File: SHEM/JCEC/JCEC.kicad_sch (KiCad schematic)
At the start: 0 parts

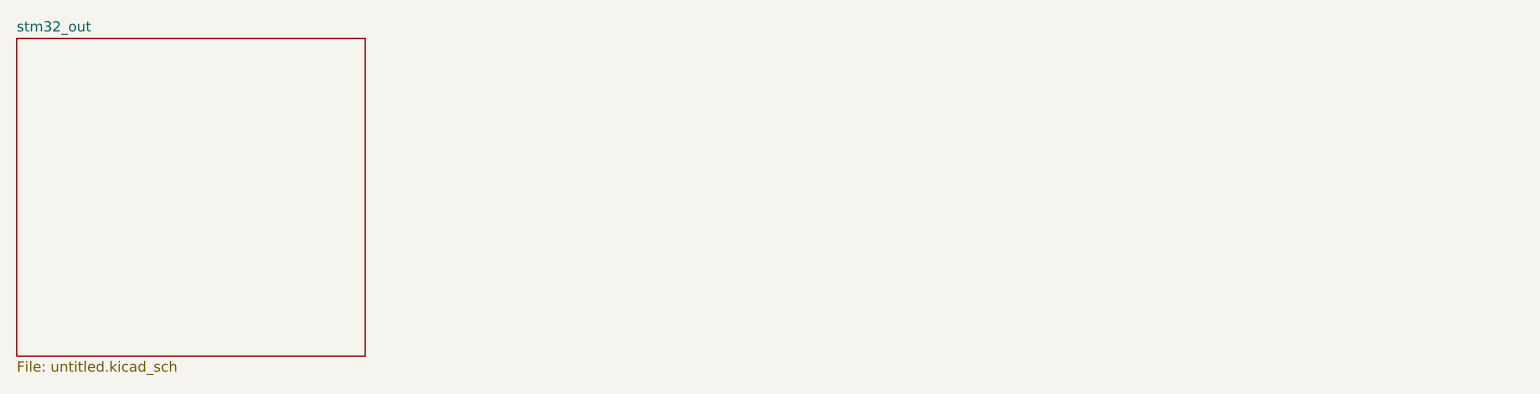
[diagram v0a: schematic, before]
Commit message: schémas updaté
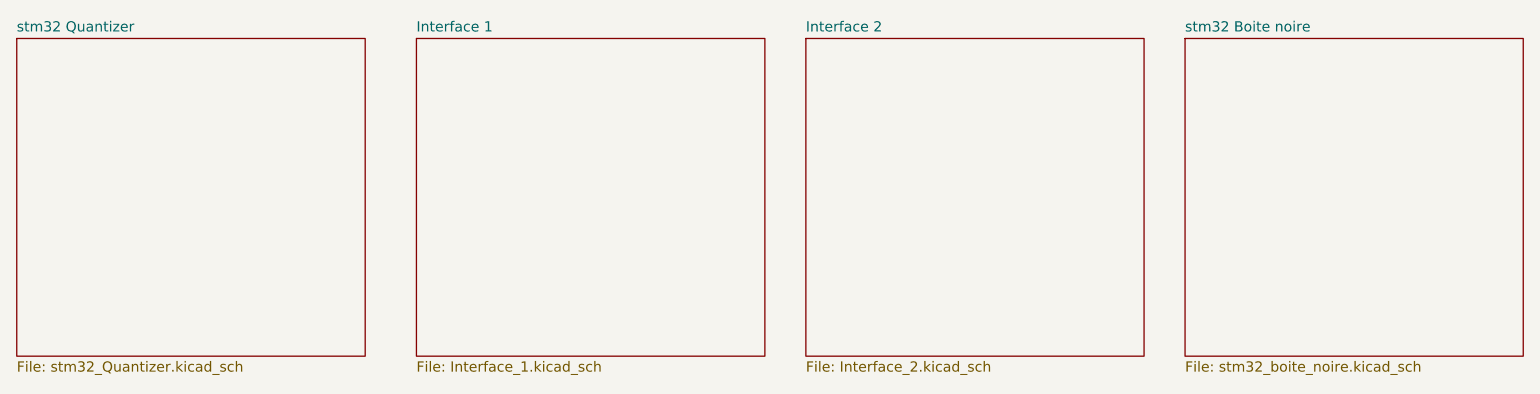
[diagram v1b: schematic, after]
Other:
- sheet stm32_out renamed stm32 Quantizer
- added sheet Interface 1 (Interface_1.kicad_sch)
- added sheet Interface 2 (Interface_2.kicad_sch)
- added sheet stm32 Boite noire (stm32_boite_noire.kicad_sch)
- sheet stm32 Quantizer: file untitled.kicad_sch -> stm32_Quantizer.kicad_sch
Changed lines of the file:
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@@
 			(color 0 0 0 0.0000)
 		)
-		(property "Sheetname" "stm32_out"
+		(property "Sheetname" "stm32 Quantizer"
 			(at 20.32 18.3384 0)
 			(effects
@@
 			)
 		)
-		(property "Sheetfile" "untitled.kicad_sch"
+		(property "Sheetfile" "stm32_Quantizer.kicad_sch"
 			(at 20.32 59.0046 0)
 			(effects
@@
 				)
 			)
+		)
+	)
+	(sheet
+		(at 69.85 19.05)
+		(size 43.18 39.37)
+		(exclude_from_sim no)
+		(in_bom yes)
+		(on_board yes)
+		(dnp no)
+		(fields_autoplaced yes)
+		(stroke
+			(width 0.1524)
+			(type solid)
+		)
+		(fill
+			(color 0 0 0 0.0000)
+		)
+		(property "Sheetname" "Interface 1"
+			(at 69.85 18.3384 0)
+			(effects
+				(font
+					(size 1.27 1.27)
+				)
+				(justify left bottom)
+			)
+		)
+		(property "Sheetfile" "Interface_1.kicad_sch"
+			(at 69.85 59.0046 0)
+			(effects
+				(font
+					(size 1.27 1.27)
+				)
+				(justify left top)
+			)
+		)
+		(instances
+			(project "JCEC"
+				(path "/0448b4c1-bd17-4072-a731-a022617275b4"
+					(page "4")
+				)
+			)
+		)
+	)
+	(sheet
+		(at 118.11 19.05)
+		(size 41.91 39.37)
+		(exclude_from_sim no)
+		(in_bom yes)
+		(on_board yes)
+		(dnp no)
+		(fields_autoplaced yes)
+		(stroke
+			(width 0.1524)
+			(type solid)
+		)
+		(fill
+			(color 0 0 0 0.0000)
+		)
+		(property "Sheetname" "Interface 2"
+			(at 118.11 18.3384 0)
+			(effects
+				(font
+					(size 1.27 1.27)
+				)
+				(justify left bottom)
+			)
+		)
+		(property "Sheetfile" "Interface_2.kicad_sch"
+			(at 118.11 59.0046 0)
+			(effects
+				(font
+					(size 1.27 1.27)
+				)
+				(justify left top)
+			)
+		)
+		(instances
+			(project "JCEC"
+				(path "/0448b4c1-bd17-4072-a731-a022617275b4"
+					(page "4")
+				)
+			)
+		)
+	)
+	(sheet
+		(at 165.1 19.05)
+		(size 41.91 39.37)
+		(exclude_from_sim no)
+		(in_bom yes)
+		(on_board yes)
+		(dnp no)
+		(fields_autoplaced yes)
+		(stroke
+			(width 0.1524)
+			(type solid)
+		)
+		(fill
+			(color 0 0 0 0.0000)
+		)
+		(property "Sheetname" "stm32 Boite noire"
+			(at 165.1 18.3384 0)
+			(effects
+				(font
+					(size 1.27 1.27)
+				)
+				(justify left bottom)
+			)
+		)
+		(property "Sheetfile" "stm32_boite_noire.kicad_sch"
+			(at 165.1 59.0046 0)
+			(effects
+				(font
+					(size 1.27 1.27)
+				)
+				(justify left top)
+			)
+		)
+		(property "Field2" ""
+			(at 165.1 19.05 0)
+			(effects
+				(font
+					(size 1.27 1.27)
+				)
+			)
+		)
+		(instances
+			(project "JCEC"
+				(path "/0448b4c1-bd17-4072-a731-a022617275b4"
+					(page "5")
+				)
+			)
